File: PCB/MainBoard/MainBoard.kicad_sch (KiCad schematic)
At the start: 16 parts, among them J1 Pi_Zero, J2 JMD0.96C, J3 WS2812, J4 Extra_Keys, J5 JoyStick_Or_I2C1, SW1 PiPowerSwitch, SW2 SPI_SW, SW3 RotaryEncoder_Switch, U1 Pico

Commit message: Added 0402 SMT capacitor
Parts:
- C1, C2: footprint Capacitor_SMD:C_1206_3216Metric_Pad1.33x1.80mm_HandSolder -> CustomCapacitor:C_1206_3216Metric_Pad1.33x1.80mm_HandSolder
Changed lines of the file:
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@@
       (effects (font (size 1.27 1.27)) (justify left))
     )
-    (property "Footprint" "Capacitor_SMD:C_1206_3216Metric_Pad1.33x1.80mm_HandSolder" (at 120.5992 150.114 0)
+    (property "Footprint" "CustomCapacitor:C_1206_3216Metric_Pad1.33x1.80mm_HandSolder" (at 120.5992 150.114 0)
       (effects (font (size 1.27 1.27)) hide)
     )
@@
       (effects (font (size 1.27 1.27)) (justify left))
     )
-    (property "Footprint" "Capacitor_SMD:C_1206_3216Metric_Pad1.33x1.80mm_HandSolder" (at 120.5992 186.944 0)
-      (effects (font (size 1.27 1.27)) hide)
-    )
+    (property "Footprint" "CustomCapacitor:C_1206_3216Metric_Pad1.33x1.80mm_HandSolder" (at 120.5992 186.944 0)
+      (effects (font (size 1.27 1.27)) hide)
+    )

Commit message: Changed the footprint and silkscreen
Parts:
- J3: footprint Connector_PinHeader_2.54mm:PinHeader_1x03_P2.54mm_Horizontal -> Connector_PinHeader_2.54mm:PinHeader_1x03_P2.54mm_Vertical
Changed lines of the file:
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@@
       (effects (font (size 1.27 1.27)) (justify left))
     )
-    (property "Footprint" "Connector_PinHeader_2.54mm:PinHeader_1x03_P2.54mm_Horizontal" (at 49.403 75.311 0)
+    (property "Footprint" "Connector_PinHeader_2.54mm:PinHeader_1x03_P2.54mm_Vertical" (at 49.403 75.311 0)
       (effects (font (size 1.27 1.27)) hide)
     )

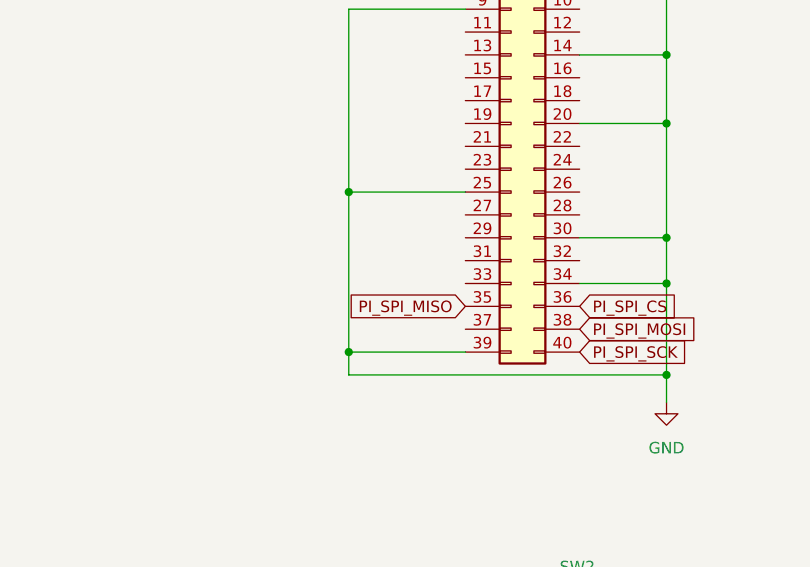
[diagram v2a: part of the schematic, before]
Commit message: Updated the footprint of the pi zero
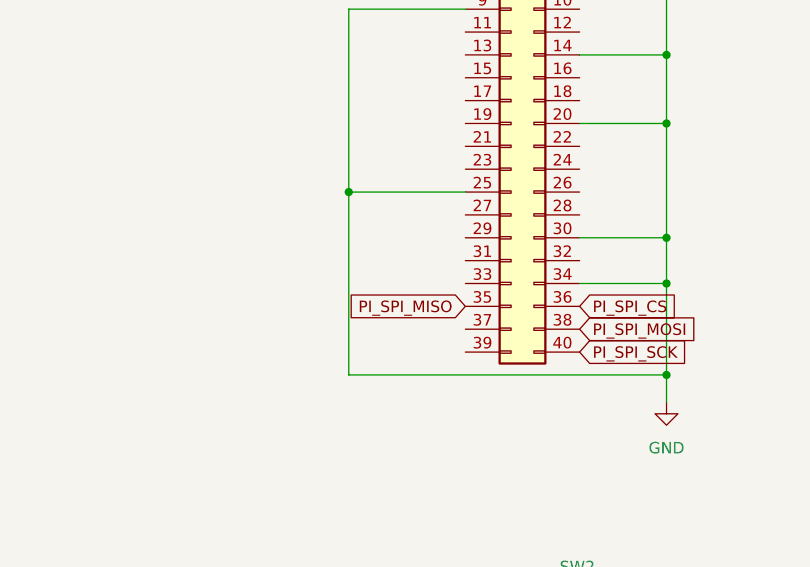
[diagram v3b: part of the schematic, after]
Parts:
- J1: footprint PiZero:Raspberry_Pi_Zero_Socketed_THT_MountingHoles_Castellated -> PiZero:Raspberry_Pi_Zero_Socketed_THT_MountingHoles_Expand
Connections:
- net GND: no longer J1.39 (Pin_39)
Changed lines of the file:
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@@
     (comment 1 "CC BY-SA 4.0")
   )
-  (junction (at 116.332 77.216) (diameter 0) (color 0 0 0 0)
-  )
   (junction (at 116.332 59.436) (diameter 0) (color 0 0 0 0)
   )
@@
     (stroke (width 0) (type default))
   )
-  (wire (pts (xy 116.332 59.436) (xy 116.332 77.216))
+  (wire (pts (xy 116.332 59.436) (xy 116.332 79.756))
     (stroke (width 0) (type default))
   )
@@
     (stroke (width 0) (type default))
   )
-  (wire (pts (xy 116.332 77.216) (xy 116.332 79.756))
-    (stroke (width 0) (type default))
-  )
   (wire (pts (xy 109.22 166.624) (xy 123.952 166.624))
     (stroke (width 0) (type default))
@@
   )
   (wire (pts (xy 116.332 39.116) (xy 116.332 59.436))
-    (stroke (width 0) (type default))
-  )
-  (wire (pts (xy 116.332 77.216) (xy 129.286 77.216))
     (stroke (width 0) (type default))
   )
@@
       (effects (font (size 1.27 1.27)))
     )
-    (property "Footprint" "PiZero:Raspberry_Pi_Zero_Socketed_THT_MountingHoles_Castellated" (at 134.366 51.816 0)
-      (effects (font (size 1.27 1.27)) hide)
-    )
+    (property "Footprint" "PiZero:Raspberry_Pi_Zero_Socketed_THT_MountingHoles_Expand" (at 134.366 51.816 0)
+      (effects (font (size 1.27 1.27)) hide)
+    )

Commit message: Minor changes
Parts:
- J1: footprint PiZero:Raspberry_Pi_Zero_Socketed_THT_MountingHoles_Expand -> PiZero:Raspberry_Pi_Zero_Socketed_THT_MountingHoles_Castellated
- R1: footprint Resistor_THT:R_Axial_DIN0207_L6.3mm_D2.5mm_P10.16mm_Horizontal -> CustomResitor:R_Axial_DIN0207_L6.3mm_D2.5mm_P10.16mm_Horizontal_0603
- R2, R3, R4, R5: footprint Resistor_THT:R_Axial_DIN0207_L6.3mm_D2.5mm_P10.16mm_Horizontal -> CustomResitor:R_Axial_DIN0207_L6.3mm_D2.5mm_P10.16mm_Horizontal_0402
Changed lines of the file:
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@@
       (effects (font (size 1.27 1.27)))
     )
-    (property "Footprint" "Resistor_THT:R_Axial_DIN0207_L6.3mm_D2.5mm_P10.16mm_Horizontal" (at 107.442 170.434 90)
+    (property "Footprint" "CustomResitor:R_Axial_DIN0207_L6.3mm_D2.5mm_P10.16mm_Horizontal_0402" (at 107.442 170.434 90)
       (effects (font (size 1.27 1.27)) hide)
     )
@@
       (effects (font (size 1.27 1.27)) (justify left))
     )
-    (property "Footprint" "Resistor_THT:R_Axial_DIN0207_L6.3mm_D2.5mm_P10.16mm_Horizontal" (at 107.442 157.734 90)
+    (property "Footprint" "CustomResitor:R_Axial_DIN0207_L6.3mm_D2.5mm_P10.16mm_Horizontal_0402" (at 107.442 157.734 90)
       (effects (font (size 1.27 1.27)) hide)
     )
@@
       (effects (font (size 1.27 1.27)))
     )
-    (property "Footprint" "Resistor_THT:R_Axial_DIN0207_L6.3mm_D2.5mm_P10.16mm_Horizontal" (at 100.584 159.766 90)
+    (property "Footprint" "CustomResitor:R_Axial_DIN0207_L6.3mm_D2.5mm_P10.16mm_Horizontal_0402" (at 100.584 159.766 90)
       (effects (font (size 1.27 1.27)) hide)
     )
@@
       (effects (font (size 1.27 1.27)))
     )
-    (property "Footprint" "PiZero:Raspberry_Pi_Zero_Socketed_THT_MountingHoles_Expand" (at 134.366 51.816 0)
+    (property "Footprint" "PiZero:Raspberry_Pi_Zero_Socketed_THT_MountingHoles_Castellated" (at 134.366 51.816 0)
       (effects (font (size 1.27 1.27)) hide)
     )
@@
       (effects (font (size 1.27 1.27)))
     )
-    (property "Footprint" "Resistor_THT:R_Axial_DIN0207_L6.3mm_D2.5mm_P10.16mm_Horizontal" (at 40.513 77.089 90)
+    (property "Footprint" "CustomResitor:R_Axial_DIN0207_L6.3mm_D2.5mm_P10.16mm_Horizontal_0603" (at 40.513 77.089 90)
       (effects (font (size 1.27 1.27)) hide)
     )
@@
       (effects (font (size 1.27 1.27)))
     )
-    (property "Footprint" "Resistor_THT:R_Axial_DIN0207_L6.3mm_D2.5mm_P10.16mm_Horizontal" (at 100.584 168.402 90)
-      (effects (font (size 1.27 1.27)) hide)
-    )
+    (property "Footprint" "CustomResitor:R_Axial_DIN0207_L6.3mm_D2.5mm_P10.16mm_Horizontal_0402" (at 100.584 168.402 90)
+      (effects (font (size 1.27 1.27)) hide)
+    )
